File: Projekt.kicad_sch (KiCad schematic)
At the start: 99 parts, among them J1 Solar, J2 Battery, J3 USB_B_Mini, J4 INTERFACE PORT, J5 FAN, J6 JTAG, J7 PRG, Q1 CSD19505KCS, Q11 CSD19505KCS, Q12 CSD19505KCS, Q13 CSD19505KCS, Q2 CSD19505KCS, Q3 CSD19505KCS, Q4 Si2306, Q5 MMBT3904 1A, Q6 MMBT3904 1A, Q7 Si2306, U1 ACS712, U10 ADS1015, U2 B1212S, U3 AMS1117-5.0, U4 AMS1117-3.3, U5 XL7005A, U6 XL7005A, U7 IR2104, U8 ESP32, U9 CH340G

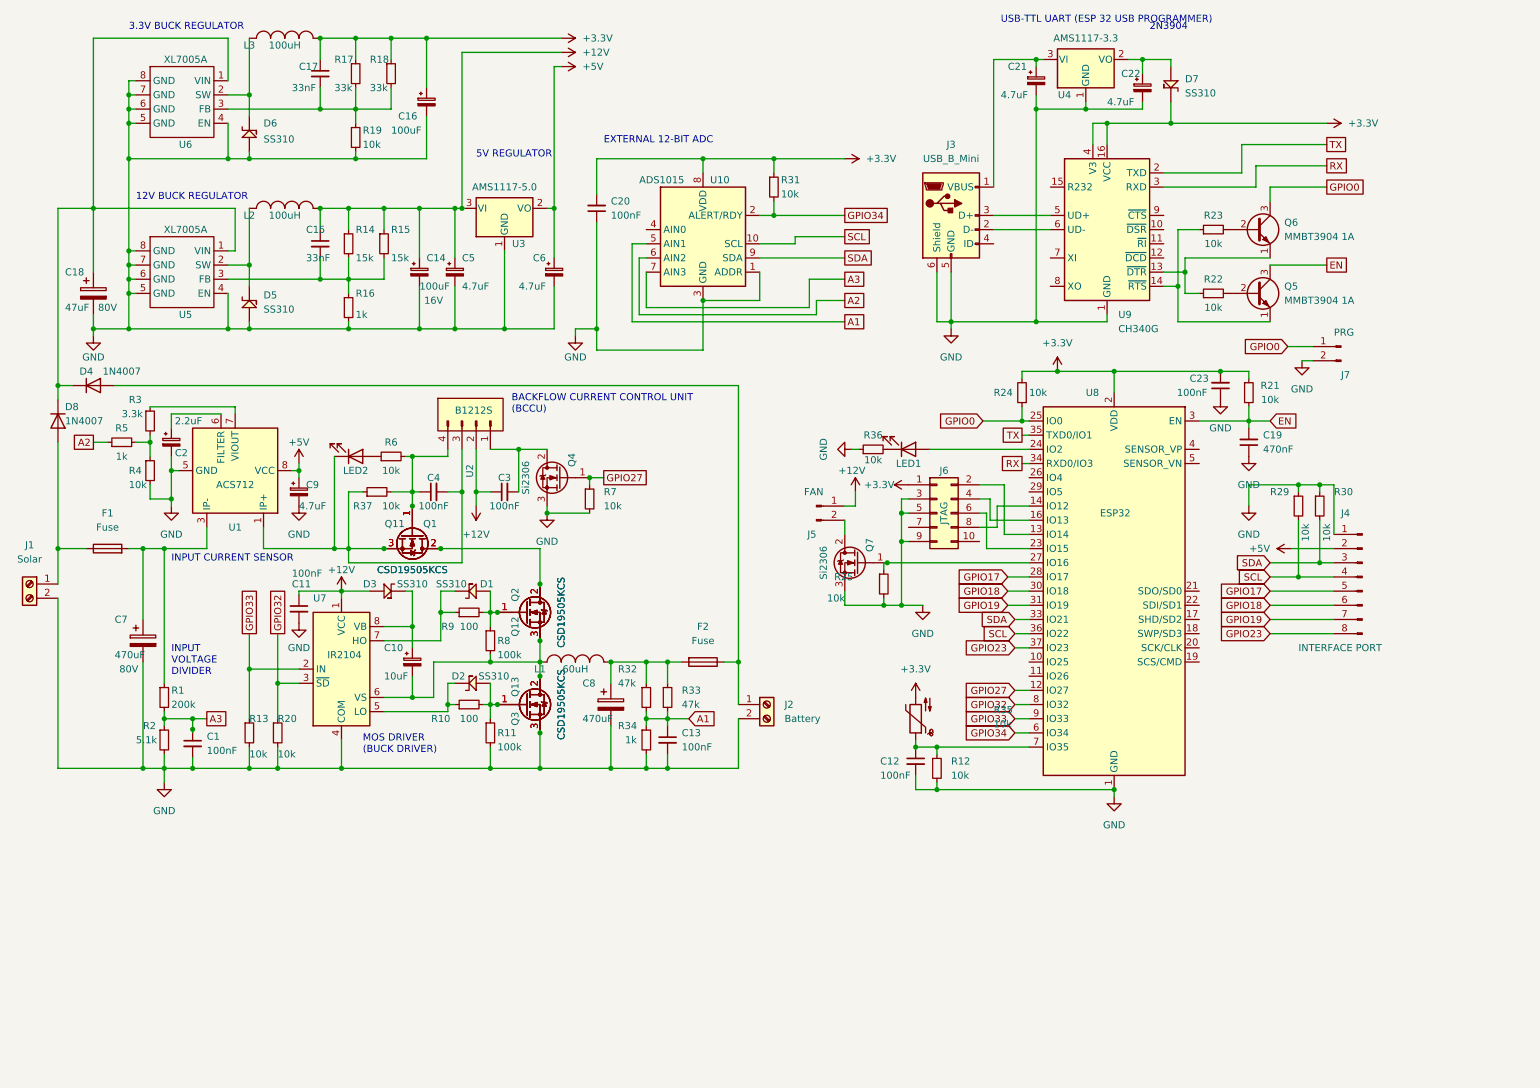
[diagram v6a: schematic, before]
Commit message: SD + RTC
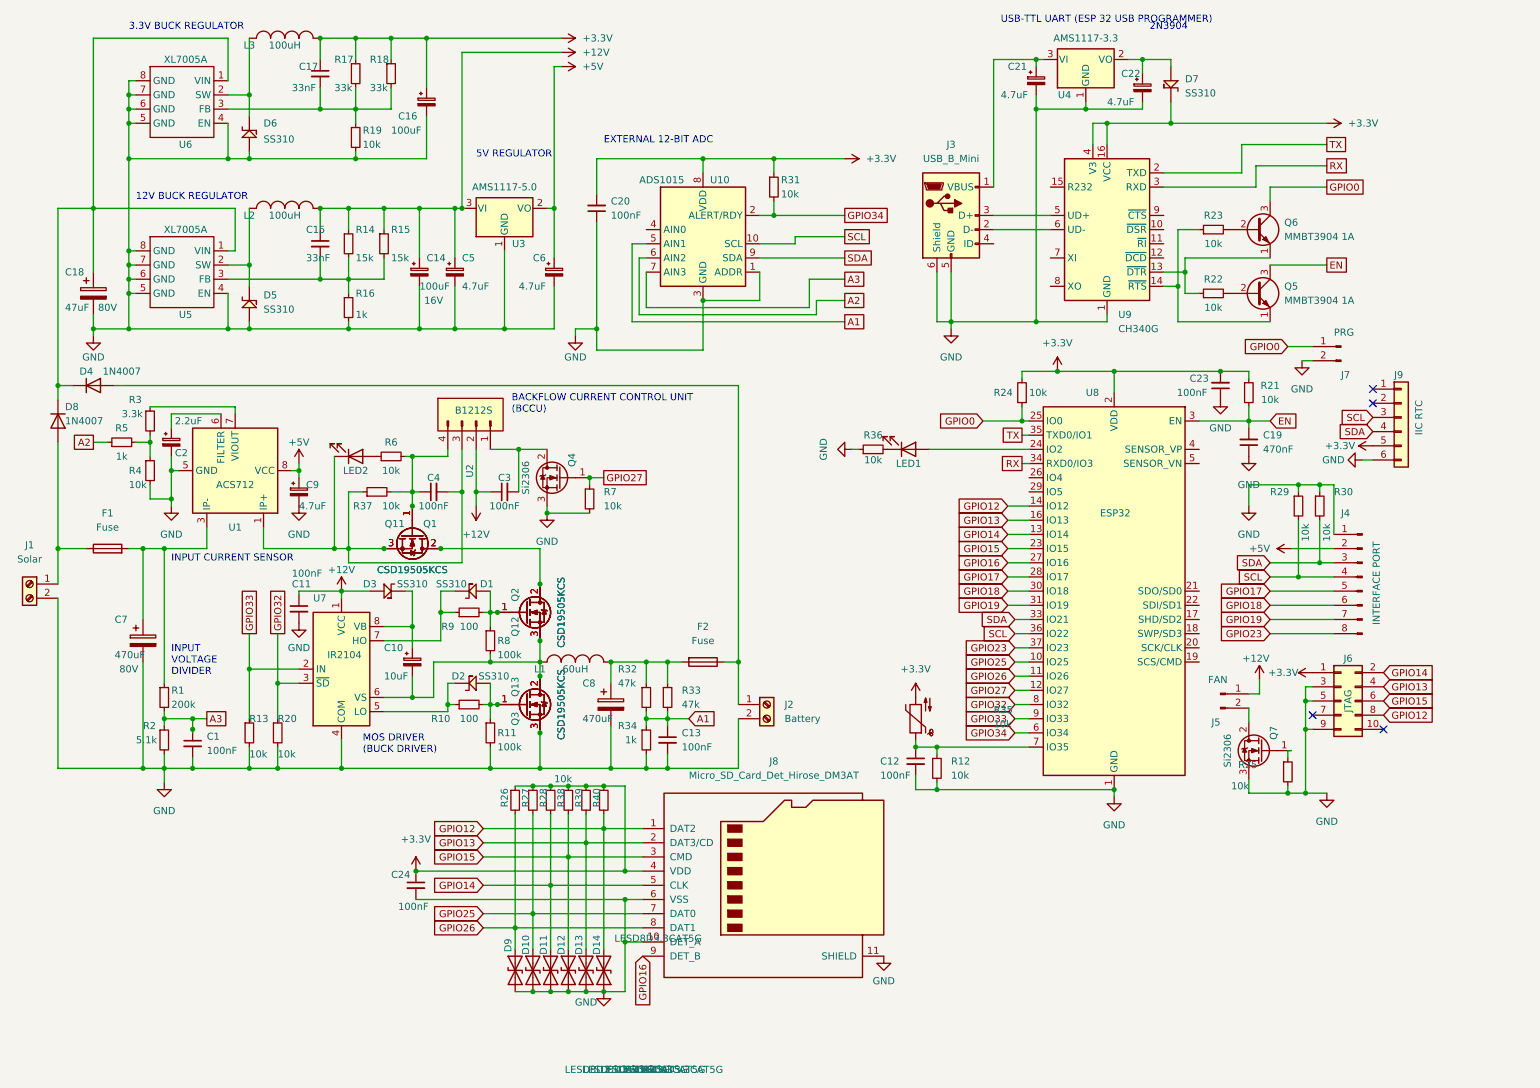
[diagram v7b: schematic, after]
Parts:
- added C24: 100nF, Capacitor_SMD:C_0603_1608Metric, symbol Device:C_Small
- added D10, D11, D12, D13, D14, D9: LESD8D3.3CAT5G, AA:SOD882D.kicad_mod, symbol Diode:1N62xxCA
- added J8: Micro_SD_Card_Det_Hirose_DM3AT, AA:microSD_HC_Molex_104031-0811, symbol Connector:Micro_SD_Card_Det_Hirose_DM3AT
- added J9: IIC RTC, Connector_PinHeader_2.54mm:PinHeader_1x06_P2.54mm_Vertical, symbol Connector_Generic:Conn_01x06
- added R26, R27, R28, R38, R39, R40: 10k, Resistor_SMD:R_0805_2012Metric, symbol Device:R_Small
- D1, D2, D3, D4, D5, D6, D7, D8: footprint Diode_SMD:D_SMB -> AA:DO-214AA
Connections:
- net +3.3V: now also C24.1, J8.4 (VDD), J9.5 (Pin_5), R26.1, R27.1, R28.1, R38.1, R39.1, R40.1
- net GND: now also C24.2, D10.1 (A1), D11.1 (A1), D12.1 (A1), D13.1 (A1), D14.1 (A1), D9.1 (A1), J8.10 (DET_A), J8.11 (SHIELD), J8.6 (VSS), J9.6 (Pin_6)
- net SCL: now also J9.3 (Pin_3)
- net SDA: now also J9.4 (Pin_4)
- net GPIO14: now reaches J6.2 (Pin_2), U8.13 (IO14)
- net GPIO14: now also D11.2 (A2), J8.5 (CLK), R28.2
- net GPIO13: now reaches J6.4 (Pin_4), U8.16 (IO13)
- net GPIO13: now also D13.2 (A2), J8.2 (DAT3/CD), R39.2
- net GPIO15: now reaches J6.6 (Pin_6), U8.23 (IO15)
- net GPIO15: now also D12.2 (A2), J8.3 (CMD), R38.2
- net GPIO12: now reaches J6.8 (Pin_8), U8.14 (IO12)
- net GPIO12: now also D14.2 (A2), J8.1 (DAT2), R40.2
- net at Q7.1 (G), R25.1: no longer U8.27 (IO16)
- net GPIO25: now reaches U8.10 (IO25)
- net GPIO25: now also D10.2 (A2), J8.7 (DAT0), R27.2
- net GPIO26: now reaches U8.11 (IO26)
- net GPIO26: now also D9.2 (A2), J8.8 (DAT1), R26.2
- new net GPIO16: J8.9 (DET_B), U8.27 (IO16)
- no-connect marks 0 -> 4
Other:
- moved on the sheet: J5, J6, Q7, R25

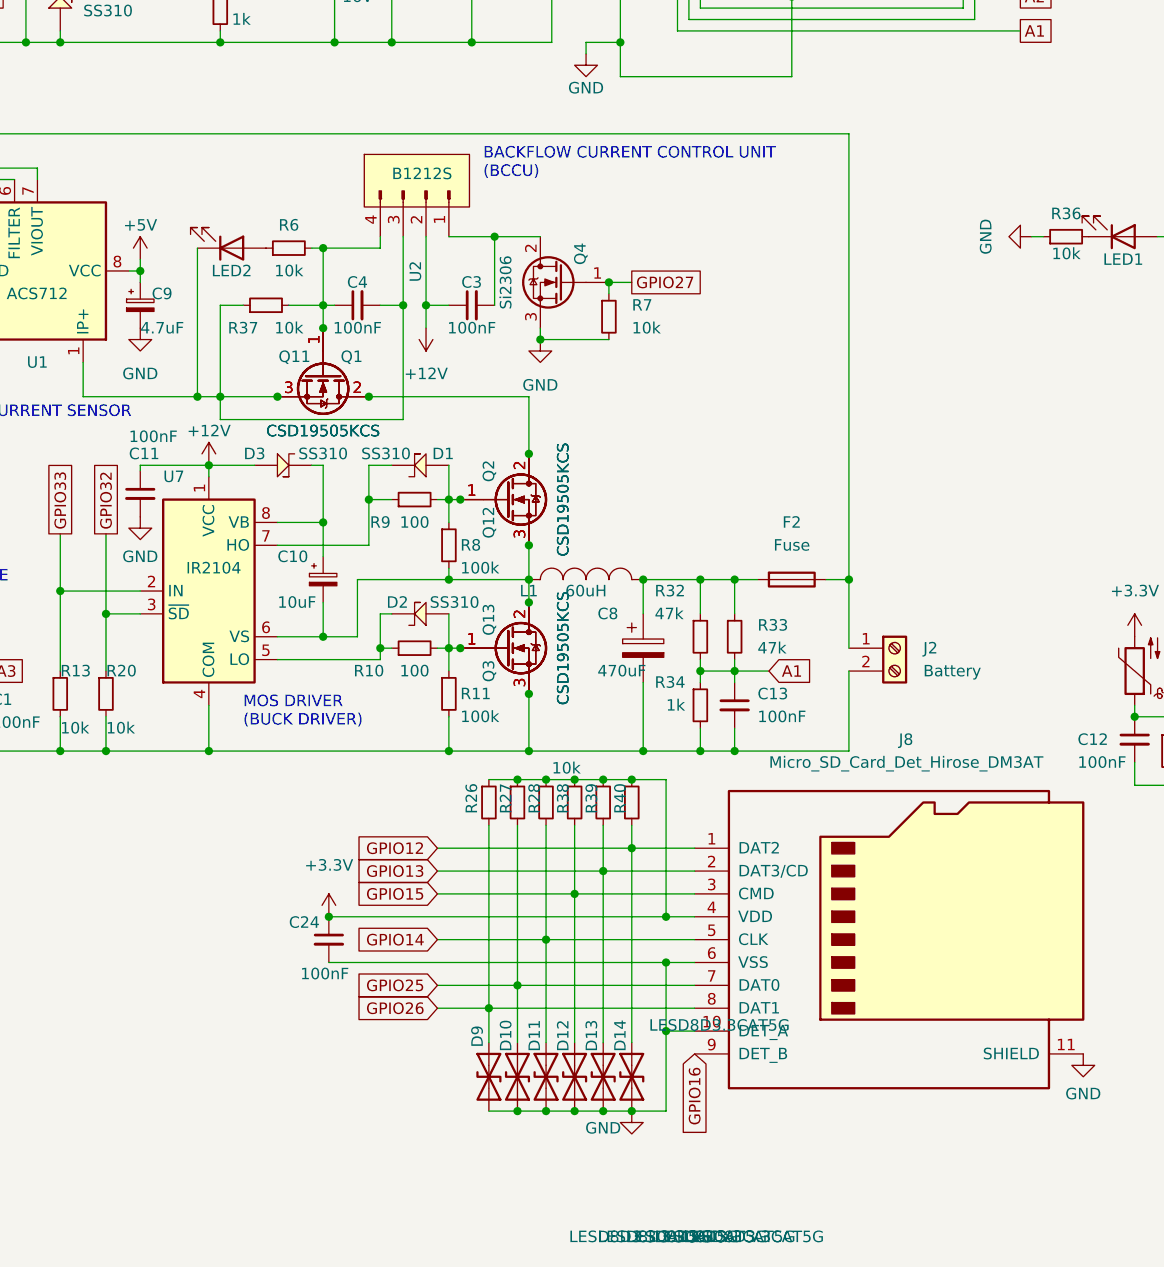
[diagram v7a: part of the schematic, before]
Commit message: 3D Modelle und Footprints vervollständigt
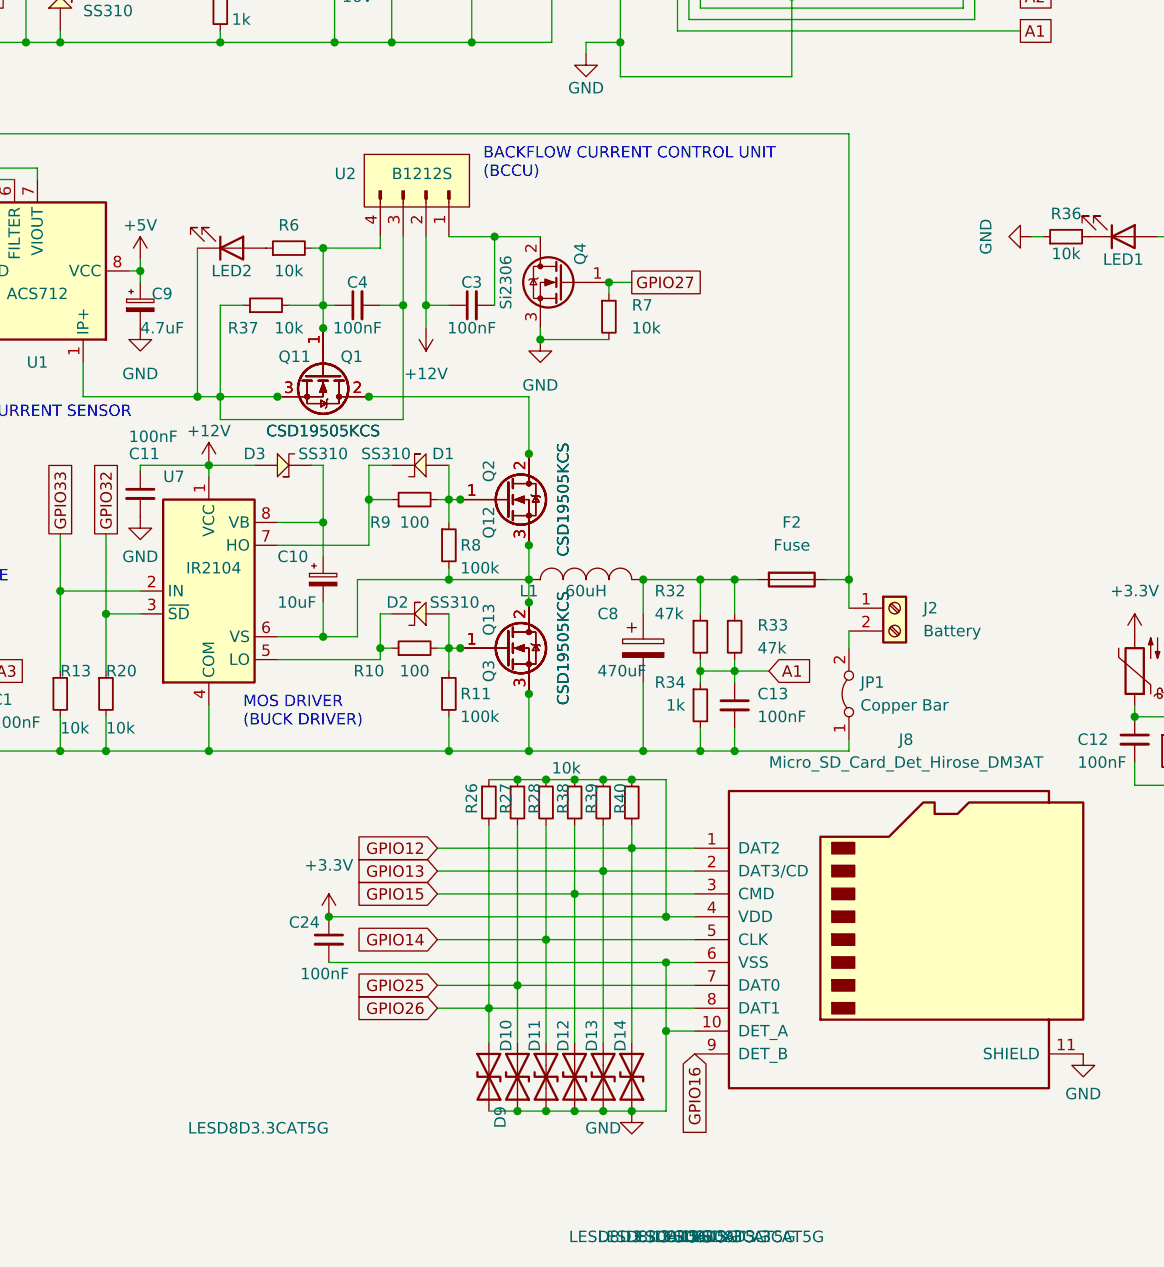
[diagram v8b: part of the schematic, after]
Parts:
- added JP1: Copper Bar, AA:COPPER_BAR, symbol Jumper:Jumper_2_Bridged
- U2: footprint Connector_PinHeader_2.54mm:PinHeader_1x04_P2.54mm_Vertical -> AA:B1212S
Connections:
- net GND: now also D9.2 (A2), JP1.1 (A); no longer D9.1 (A1), J2.2 (Pin_2)
- net GPIO26: now also D9.1 (A1); no longer D9.2 (A2)
- new net: J2.2 (Pin_2), JP1.2 (B)
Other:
- moved on the sheet: D9, J2
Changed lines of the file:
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@@
     (stroke (width 0) (type default) (color 0 0 0 0))
   )
-  (wire (pts (xy 142.24 146.05) (xy 142.24 154.94))
-    (stroke (width 0) (type default) (color 0 0 0 0))
-  )
   (wire (pts (xy 35.56 115.57) (xy 39.37 115.57))
     (stroke (width 0) (type default) (color 0 0 0 0))
@@
     (stroke (width 0) (type default) (color 0 0 0 0))
   )
-  (wire (pts (xy 142.24 135.89) (xy 142.24 143.51))
+  (wire (pts (xy 142.24 135.89) (xy 142.24 139.065))
     (stroke (width 0) (type default) (color 0 0 0 0))
   )
@@
     (stroke (width 0) (type default) (color 0 0 0 0))
   )
+  (wire (pts (xy 142.24 153.67) (xy 142.24 154.94))
+    (stroke (width 0) (type default) (color 0 0 0 0))
+  )
   (wire (pts (xy 125.73 135.89) (xy 125.73 139.7))
     (stroke (width 0) (type default) (color 0 0 0 0))
@@
     (stroke (width 0) (type default) (color 0 0 0 0))
   )
+  (wire (pts (xy 142.24 141.605) (xy 142.24 143.51))
+    (stroke (width 0) (type default) (color 0 0 0 0))
+  )
   (wire (pts (xy 124.46 63.5) (xy 124.46 73.66))
     (stroke (width 0) (type default) (color 0 0 0 0))
@@
     (pin "2")
   )
-  (symbol (lib_id "Diode:1N62xxCA") (at 102.235 191.135 90) (unit 1)
+  (symbol (lib_id "Diode:1N62xxCA") (at 102.235 191.135 270) (unit 1)
     (in_bom yes) (on_board yes)
-    (property "Reference" "D9" (id 0) (at 100.965 185.42 0)
+    (property "Reference" "D9" (id 0) (at 103.505 196.85 0)
       (effects (font (size 1.27 1.27)) (justify right))
     )
-    (property "Value" "LESD8D3.3CAT5G" (id 1) (at 120.015 185.42 90)
+    (property "Value" "LESD8D3.3CAT5G" (id 1) (at 84.455 196.85 90)
       (effects (font (size 1.27 1.27)) (justify right))
     )
-    (property "Footprint" "AA:SOD882D.kicad_mod" (id 2) (at 97.155 191.135 0)
+    (property "Footprint" "AA:SOD882D.kicad_mod" (id 2) (at 107.315 191.135 0)
       (effects (font (size 1.27 1.27)) hide)
     )
-    (property "Datasheet" "https://www.vishay.com/docs/88301/15ke.pdf" (id 3) (at 104.775 191.135 0)
+    (property "Datasheet" "https://www.vishay.com/docs/88301/15ke.pdf" (id 3) (at 99.695 191.135 0)
       (effects (font (size 1.27 1.27)) hide)
     )
@@
     (pin "1")
   )
+  (symbol (lib_id "Jumper:Jumper_2_Bridged") (at 142.24 148.59 90) (unit 1)
+    (in_bom yes) (on_board yes) (fields_autoplaced)
+    (property "Reference" "JP1" (id 0) (at 143.51 147.3199 90)
+      (effects (font (size 1.27 1.27)) (justify right))
+    )
+    (property "Value" "Copper Bar" (id 1) (at 143.51 149.8599 90)
+      (effects (font (size 1.27 1.27)) (justify right))
+    )
+    (property "Footprint" "AA:COPPER_BAR" (id 2) (at 142.24 148.59 0)
+      (effects (font (size 1.27 1.27)) hide)
+    )
+    (property "Datasheet" "~" (id 3) (at 142.24 148.59 0)
+      (effects (font (size 1.27 1.27)) hide)
+    )
+    (pin "1")
+    (pin "2")
+  )
   (symbol (lib_id "Device:R_Small") (at 105.41 160.655 0) (unit 1)
     (in_bom yes) (on_board yes)
@@
   (symbol (lib_id "footprint:B1212S") (at 95.25 92.71 270) (unit 1)
     (in_bom yes) (on_board yes)
-    (property "Reference" "U2" (id 0) (at 94.107 100.457 0)
+    (property "Reference" "U2" (id 0) (at 85.09 90.805 90)
       (effects (font (size 1.27 1.27)) (justify left))
     )
@@
       (effects (font (size 1.27 1.27)) (justify left))
     )
-    (property "Footprint" "Connector_PinHeader_2.54mm:PinHeader_1x04_P2.54mm_Vertical" (id 2) (at 95.504 82.042 0)
+    (property "Footprint" "AA:B1212S" (id 2) (at 95.504 82.042 0)
       (effects (font (size 1.27 1.27)) hide)
     )
@@
     (pin "2")
   )
-  (symbol (lib_id "Connector:Screw_Terminal_01x02") (at 147.32 143.51 0) (unit 1)
+  (symbol (lib_id "Connector:Screw_Terminal_01x02") (at 147.32 139.065 0) (unit 1)
     (in_bom yes) (on_board yes) (fields_autoplaced)
-    (property "Reference" "J2" (id 0) (at 150.495 143.5099 0)
+    (property "Reference" "J2" (id 0) (at 150.495 139.0649 0)
       (effects (font (size 1.27 1.27)) (justify left))
     )
-    (property "Value" "Battery" (id 1) (at 150.495 146.0499 0)
+    (property "Value" "Battery" (id 1) (at 150.495 141.6049 0)
       (effects (font (size 1.27 1.27)) (justify left))
     )
-    (property "Footprint" "footprints:TerminalBlock_DEGSON_DG135T" (id 2) (at 147.32 143.51 0)
+    (property "Footprint" "footprints:TerminalBlock_DEGSON_DG135T" (id 2) (at 147.32 139.065 0)
       (effects (font (size 1.27 1.27)) hide)
     )
-    (property "Datasheet" "~" (id 3) (at 147.32 143.51 0)
+    (property "Datasheet" "~" (id 3) (at 147.32 139.065 0)
       (effects (font (size 1.27 1.27)) hide)
     )
@@
       (reference "J9") (unit 1) (value "IIC RTC") (footprint "Connector_PinHeader_2.54mm:PinHeader_1x06_P2.54mm_Vertical")
     )
+    (path "/44ab99b2-7446-4648-936b-b437d5fec253"
+      (reference "JP1") (unit 1) (value "Copper Bar") (footprint "AA:COPPER_BAR")
+    )
     (path "/a34be4f0-cd07-4bab-9f46-bdfef665e51a"
       (reference "L1") (unit 1) (value "60uH") (footprint "Inductor_THT:L_Toroid_Vertical_L21.6mm_W11.4mm_P7.62mm_Pulse_KM-3")
@@
     )
     (path "/cdb8942e-f0a4-4ac1-90cf-1b9ac48e7336"
-      (reference "U2") (unit 1) (value "B1212S") (footprint "Connector_PinHeader_2.54mm:PinHeader_1x04_P2.54mm_Vertical")
+      (reference "U2") (unit 1) (value "B1212S") (footprint "AA:B1212S")
     )
     (path "/67742da5-6a1f-4347-b971-97221228ab82"
